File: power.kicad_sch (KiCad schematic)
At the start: 13 parts, among them U3 BQ24075, U4 XC6220B331MR, U5 LN4913

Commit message: final?
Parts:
- removed JP6: Jumper_3_Open, Jumper:SolderJumper-3_P2.0mm_Open_TrianglePad1.0x1.5mm_NumberLabels, symbol Jumper:Jumper_3_Open
- added SW2: SW_SPDT, Button_Switch_SMD:SW_SPDT_PCM12, symbol Switch:SW_SPDT
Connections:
- net VDDH: now also SW2.3 (C)
- net MAGNET: now reaches R10.2, U5.2 (VOUT)
- net MAGNET: now also SW2.1 (A)
- net at U4.3 (CE): now also SW2.2 (B)
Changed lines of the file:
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@@
   (junction (at 74.93 106.68) (diameter 1.016) (color 0 0 0 0))
   (junction (at 74.93 127) (diameter 1.016) (color 0 0 0 0))
-  (junction (at 85.09 116.84) (diameter 1.016) (color 0 0 0 0))
   (junction (at 130.81 64.77) (diameter 1.016) (color 0 0 0 0))
   (junction (at 130.81 72.39) (diameter 1.016) (color 0 0 0 0))
@@
     (stroke (width 0) (type solid) (color 0 0 0 0))
   )
-  (wire (pts (xy 85.09 116.84) (xy 102.87 116.84))
-    (stroke (width 0) (type solid) (color 0 0 0 0))
-  )
-  (wire (pts (xy 102.87 99.06) (xy 102.87 100.33))
-    (stroke (width 0) (type solid) (color 0 0 0 0))
-  )
-  (wire (pts (xy 102.87 99.06) (xy 113.03 99.06))
-    (stroke (width 0) (type solid) (color 0 0 0 0))
-  )
-  (wire (pts (xy 102.87 116.84) (xy 102.87 113.03))
-    (stroke (width 0) (type solid) (color 0 0 0 0))
-  )
   (wire (pts (xy 106.68 106.68) (xy 113.03 106.68))
-    (stroke (width 0) (type solid) (color 0 0 0 0))
-  )
-  (wire (pts (xy 113.03 101.6) (xy 113.03 99.06))
     (stroke (width 0) (type solid) (color 0 0 0 0))
   )
@@
     (property "Intersheet References" "${INTERSHEET_REFS}" (id 0) (at 74.8506 99.3079 90)
       (effects (font (size 1.27 1.27)) (justify left) hide)
+    )
+  )
+  (global_label "VDDH" (shape input) (at 96.52 104.14 180) (fields_autoplaced)
+    (effects (font (size 1.27 1.27)) (justify right))
+    (property "Intersheet References" "${INTERSHEET_REFS}" (id 0) (at 89.1479 104.2194 0)
+      (effects (font (size 1.27 1.27)) (justify right) hide)
     )
   )
@@
     )
   )
-  (hierarchical_label "GND" (shape input) (at 76.2 77.47 180)
+  (hierarchical_label "MAGNET" (shape output) (at 85.09 116.84 0)
+    (effects (font (size 1.27 1.27)) (justify left))
+  )
+  (hierarchical_label "MAGNET" (shape output) (at 96.52 109.22 270)
     (effects (font (size 1.27 1.27)) (justify right))
   )
@@
     )
     (property "Datasheet" "" (id 3) (at 74.93 127 0)
-      (effects (font (size 1.27 1.27)) hide)
-    )
-    (pin "1")
-  )
-  (symbol (lib_id "power:GND") (at 76.2 77.47 90) (unit 1)
-    (in_bom yes) (on_board yes)
-    (property "Reference" "#PWR0128" (id 0) (at 82.55 77.47 0)
-      (effects (font (size 1.27 1.27)) hide)
-    )
-    (property "Value" "GND" (id 1) (at 80.5942 77.343 0))
-    (property "Footprint" "" (id 2) (at 76.2 77.47 0)
-      (effects (font (size 1.27 1.27)) hide)
-    )
-    (property "Datasheet" "" (id 3) (at 76.2 77.47 0)
       (effects (font (size 1.27 1.27)) hide)
     )
@@
     (pin "2")
   )
-  (symbol (lib_id "Jumper:Jumper_3_Open") (at 102.87 106.68 90) (unit 1)
-    (in_bom yes) (on_board yes)
-    (property "Reference" "JP6" (id 0) (at 99.4664 108.4591 90)
-      (effects (font (size 1.27 1.27)) (justify left))
-    )
-    (property "Value" "Jumper_3_Open" (id 1) (at 99.4664 103.1378 90)
-      (effects (font (size 1.27 1.27)) (justify left))
-    )
-    (property "Footprint" "Jumper:SolderJumper-3_P2.0mm_Open_TrianglePad1.0x1.5mm_NumberLabels" (id 2) (at 102.87 106.68 0)
-      (effects (font (size 1.27 1.27)) hide)
-    )
-    (property "Datasheet" "~" (id 3) (at 102.87 106.68 0)
-      (effects (font (size 1.27 1.27)) hide)
-    )
+  (symbol (lib_id "Switch:SW_SPDT") (at 101.6 106.68 180) (unit 1)
+    (in_bom yes) (on_board yes) (fields_autoplaced)
+    (property "Reference" "SW2" (id 0) (at 101.6 99.7924 0))
+    (property "Value" "SW_SPDT" (id 1) (at 101.6 102.5675 0))
+    (property "Footprint" "Button_Switch_SMD:SW_SPDT_PCM12" (id 2) (at 101.6 106.68 0)
+      (effects (font (size 1.27 1.27)) hide)
+    )
+    (property "Datasheet" "~" (id 3) (at 101.6 106.68 0)
+      (effects (font (size 1.27 1.27)) hide)
+    )

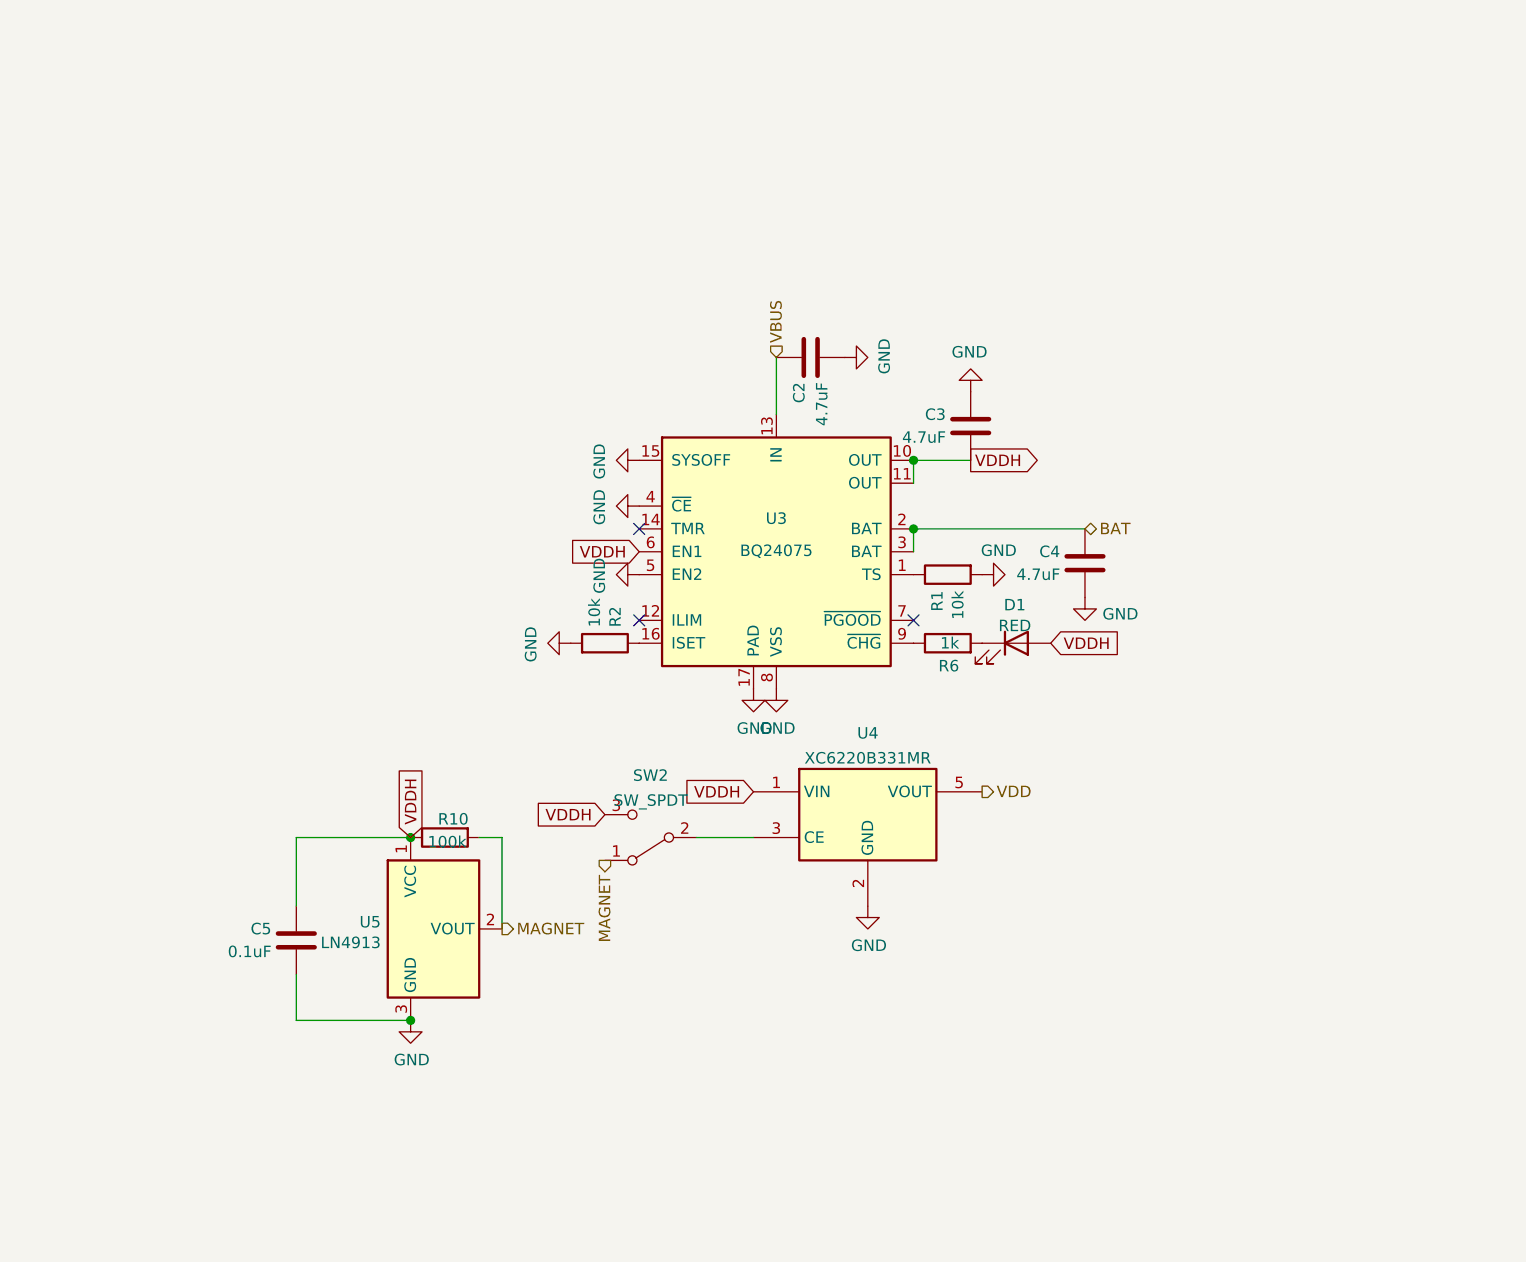
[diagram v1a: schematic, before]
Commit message: update PCB
use cirque trackpad, increase angle to 22.5
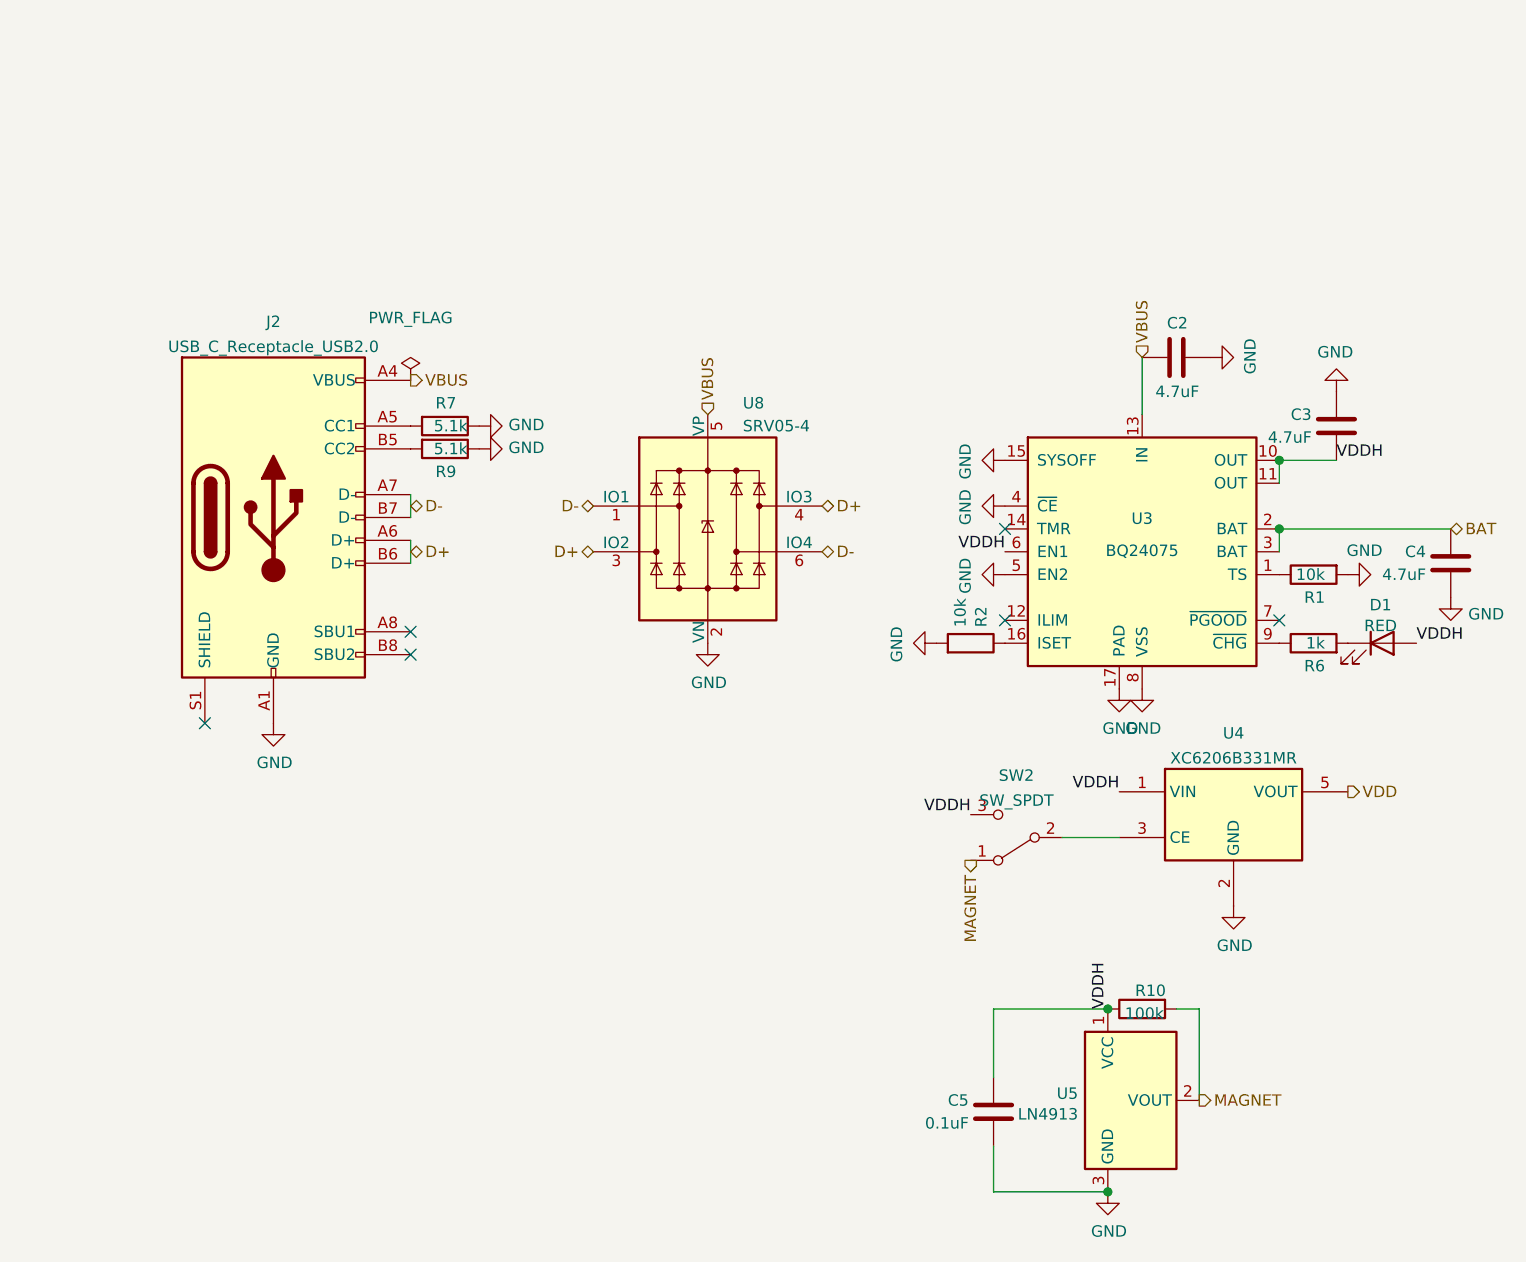
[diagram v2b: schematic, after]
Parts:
- added J2: USB_C_Receptacle_USB2.0, Connector_USB:USB_C_Receptacle_HRO_TYPE-C-31-M-12, symbol Connector:USB_C_Receptacle_USB2.0
- added R7, R9: 5.1k, Resistor_SMD:R_0603_1608Metric, symbol Device:R
- added U8: SRV05-4, Package_TO_SOT_SMD:SOT-23-6, symbol Power_Protection:SRV05-4
- U4: value XC6220B331MR -> XC6206B331MR
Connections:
- net GND: now also J2.A1 (GND), J2.A12 (GND), J2.B1 (GND), J2.B12 (GND), R7.1, R9.1, U8.2 (VN)
- net VBUS: now also J2.A4 (VBUS), J2.A9 (VBUS), J2.B4 (VBUS), J2.B9 (VBUS), U8.5 (VP)
- new net: J2.A5 (CC1), R7.2
- new net: J2.B5 (CC2), R9.2
- new net D+: J2.A6 (D+), J2.B6 (D+), U8.3 (IO2), U8.4 (IO3)
- new net D-: J2.A7 (D-), J2.B7 (D-), U8.1 (IO1), U8.6 (IO4)
- no-connect marks 3 -> 6
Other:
- moved on the sheet: C2, C3, C4, C5, D1, R1, R10, R2, R6, SW2, U3, U4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

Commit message: backup & remove useless things
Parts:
- removed C2, C3, C4: 4.7uF, Capacitor_SMD:C_0603_1608Metric, symbol Device:C
- removed D1: RED, LED_SMD:LED_0805_2012Metric, symbol Device:LED
- removed R1, R2: 10k, Resistor_SMD:R_0603_1608Metric, symbol Device:R
- removed R6: 1k, Resistor_SMD:R_0603_1608Metric, symbol Device:R
- removed U3: BQ24075, Package_DFN_QFN:VQFN-16-1EP_3x3mm_P0.5mm_EP1.68x1.68mm_ThermalVias, symbol Battery_Management:BQ24075
- removed U4: XC6206B331MR, Package_TO_SOT_SMD:SOT-23-5, symbol Regulator_Linear:XC6220B331MR
- added D1: D, Diode_SMD:D_SOD-123, symbol Device:D
- added JP3: SolderJumper_3_Open, Jumper:SolderJumper-3_P1.3mm_Open_RoundedPad1.0x1.5mm, symbol Jumper:SolderJumper_3_Open
- added Q1: AO3401A, Package_TO_SOT_SMD:SOT-23, symbol Transistor_FET:AO3401A
- added Q2: AO3400A, Package_TO_SOT_SMD:SOT-23, symbol Transistor_FET:AO3400A
- added R23: 10M, Resistor_SMD:R_0603_1608Metric, symbol Device:R
- added R3, R5: 22, Resistor_SMD:R_0603_1608Metric, symbol Device:R
- added U2: XC6220B331MR, Package_TO_SOT_SMD:SOT-23-5, symbol Regulator_Linear:XC6220B331MR
- added U3: TLV70237_SOT23-5, Package_TO_SOT_SMD:SOT-23-5, symbol Regulator_Linear:TLV70237_SOT23-5
- R9: renamed from R10; value 100k -> 1M
- renumbered C5 to C1, R9 to R8, SW2 to SW1, U5 to U4, U8 to U5
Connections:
- net GND: now also Q2.2 (S), U2.2 (GND), U3.2 (GND)
- net VBUS: now also U3.1 (IN), U3.3 (EN)
- net VDDH: now also Q1.3 (D); no longer C1.1, R9.1, SW1.3 (C), U4.1 (VCC)
- net at SW1.2 (B): now also JP3.2 (C)
- new net: Q1.1 (G), Q2.3 (D), R23.1
- new net: D1.1 (K), R3.1, R5.1
- new net: D1.2 (A), U3.5 (OUT)
- new net 3V3: U2.5 (VOUT)
- new net 3V3_EN: JP3.3 (B), U2.3 (CE)
- new net CAP: R3.2, R5.2
- new net SOLAR_OUT: C1.1, Q1.2 (S), R23.2, R9.1, SW1.3 (C), U2.1 (VIN), U4.1 (VCC)
- new net VDDH_EN: JP3.1 (A), Q2.1 (G)
- no-connect marks 6 -> 3
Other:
- moved on the sheet: C1, J2, R7, R8, R9, SW1, U4, U5
